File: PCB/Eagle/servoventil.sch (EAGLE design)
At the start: 0 parts

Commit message: Rozdělané schéma
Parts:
- added C1, C2: 100n 1206, rcl:C-EUC1206
- added D1: LOW BAT 1206, SparkFun-LED:LED1206
- added D2: STTH4R02S DO214AB, diode:DIODE-DO214AA
- added DIP: DIP-4X_DIP, #PaJa_prepinace:DIP-4X_DIP
- added F1: 3,5A 1206, adafruit:PTCFUSE-1206
- added IO1: ATTINY1634 SO20W, bt_avr:ATTINY1634-SU
- added IO2: MCP1825 SOT223, bt_regulator:MCP1825_SOT223
- added IO3: DS3231MZ+, SamacSys_Parts:DS3231MZ+
- added J1: ICSP 2x5, SparkFun-Connectors:AVR_SPI_PROG_5X2LOCK
- added J2: SERIAL, #PaJa_konektory:S1G5_JUMP
- added K1: ARK500/2, #PaJa_konektory:ARK500/2
- added R1, R8: 10k 1206, rcl:R-EU_R1206
- added R10, R9: 4k7 1206, rcl:R-EU_R1206
- added R2: 10k 1203, rcl:R-EU_R1206
- added R3: 1k 1206, rcl:R-EU_R1206
- added R4: 47k 1206, rcl:R-EU_R1206
- added R5: 2k7 1206, rcl:R-EU_R1206
- added R6: 3k3 1206, rcl:R-EU_R1206
- added R7: 100R 1206, rcl:R-EU_R1206
- added S1: 6x6mm SMD, SparkFun-Switches:MOMENTARY-SWITCH-SPST-SMD-6.2MM-TALL
- added T1: DMP2100U SOT23, bt_transistor:MOSFET-P-SOT23
- added T2: IRF7416PBF SO8, SamacSys_Parts:IRF7416PBF
- added T3: FDV303N SOT23, bt_transistor:MOSFET-N-SOT23
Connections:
- new net 3,3V_VCC: C2.1, IO2.VOUT, IO3.VCC, R10.1, R9.1
- new net 6V: C1.1, IO2.VIN, R5.2, T1.D
- new net GND: C1.2, C2.2, D1.C, D2.A, DIP.1, DIP.2, DIP.3, DIP.4, IO1.GND, IO3.GND, J1.GND@1, J1.GND@2, J1.GND@3, J1.GND@4, J2.1, K1.K1, R4.1, R6.1, S1.1, T3.S
- new net HEATSINK: IO2.GND, IO2.HEATSINK
- new net LED_LOWBAT_PIN: R7.1
- new net LOW_BAT_PIN: R5.1, R6.2
- new net N$1: F1.2, K1.K2
- new net N$10: IO3.!INT!/SQW
- new net N$12: D1.A, R7.2
- new net N$2: D2.C, F1.1, R1.2, R2.2, T1.S, T2.S_1, T2.S_2, T2.S_3
- new net N$3: R3.2, R4.2, T3.G
- new net N$5: J1.SCK
- new net N$6: J1.MISO
- new net N$7: J1.MOSI
- new net PWR_ON_PIN: R3.1
- new net PWR_RTC_ON: R1.1, S1.2, T1.G, T3.D
- new net PWR_SERVO_ON_PIN: R2.1, T2.G
- new net PWR_SERVO_OUT: T2.D_1, T2.D_2, T2.D_3, T2.D_4
- new net RESET: IO1.(RESET/DW/PCINT15)PC3, J1.RESET, J2.5, R8.2
- new net RX_PIN: J2.4
- new net SCL_PIN: IO3.SCL, R9.2
- new net SDA_PIN: IO3.SDA, R10.2
- new net SW1_PIN: DIP.8
- new net SW2_PIN: DIP.7
- new net SW3_PIN: DIP.6
- new net SW4_PIN: DIP.5
- new net TX_PIN: J2.3
- new net VCC: IO1.VCC, J1.VCC, J2.2, R8.1
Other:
- note added: "+ 0V"
- note added: "Baterie (5x AA 1,2V)"
- note added: "CPU"
- note added: "GND 3,3V TX RX RESET"
- note added: "PWR ON"
- note added: "RTC"
- note added: "ZDROJ"

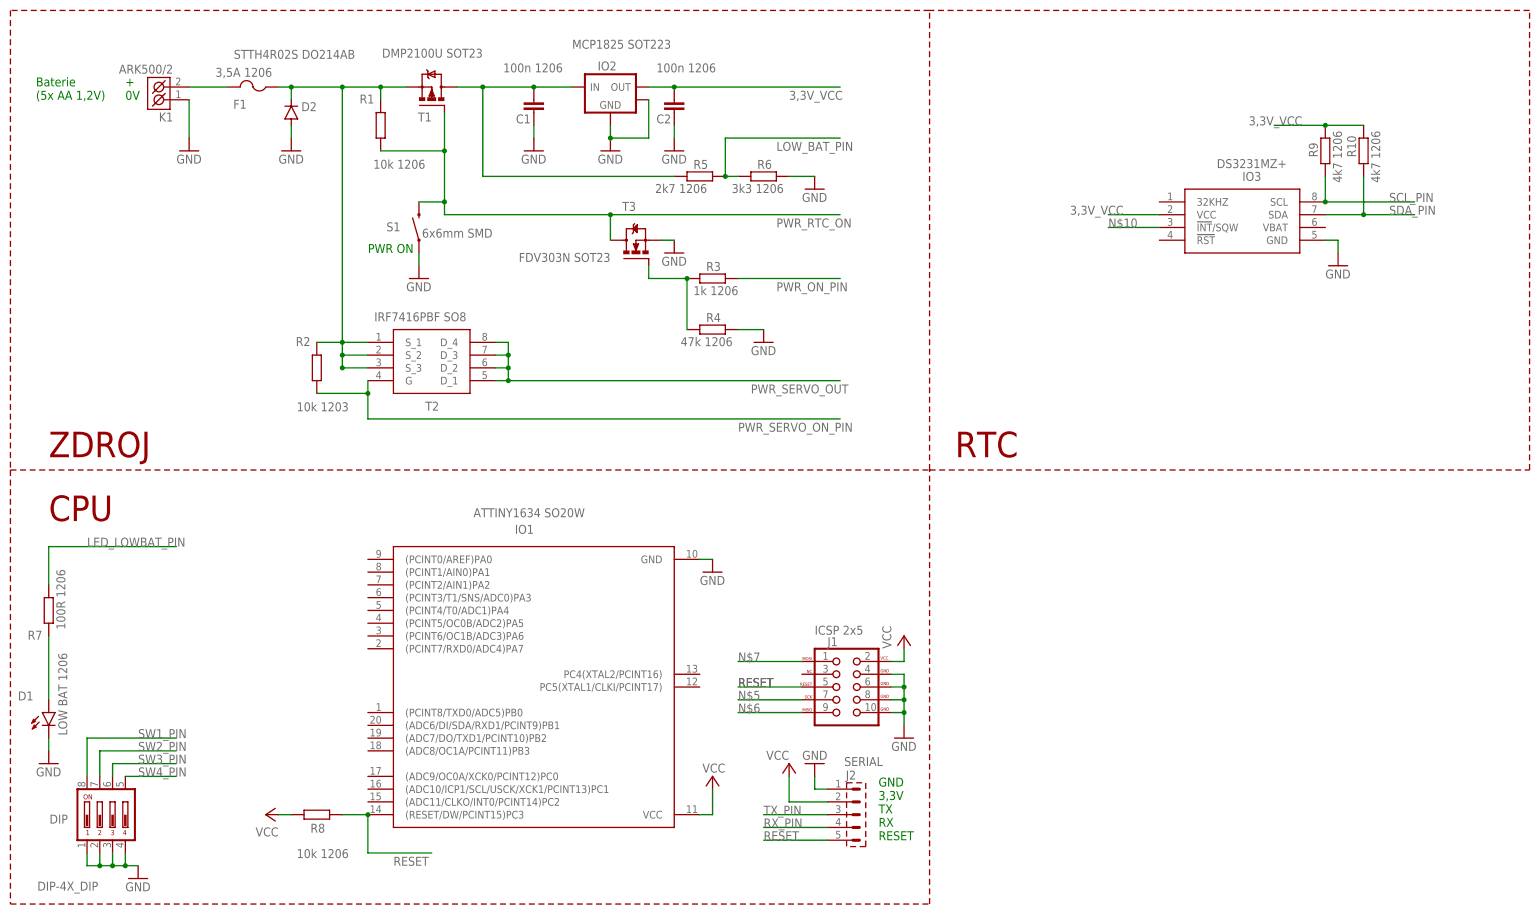
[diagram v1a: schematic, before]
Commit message: Schema před kontrolou
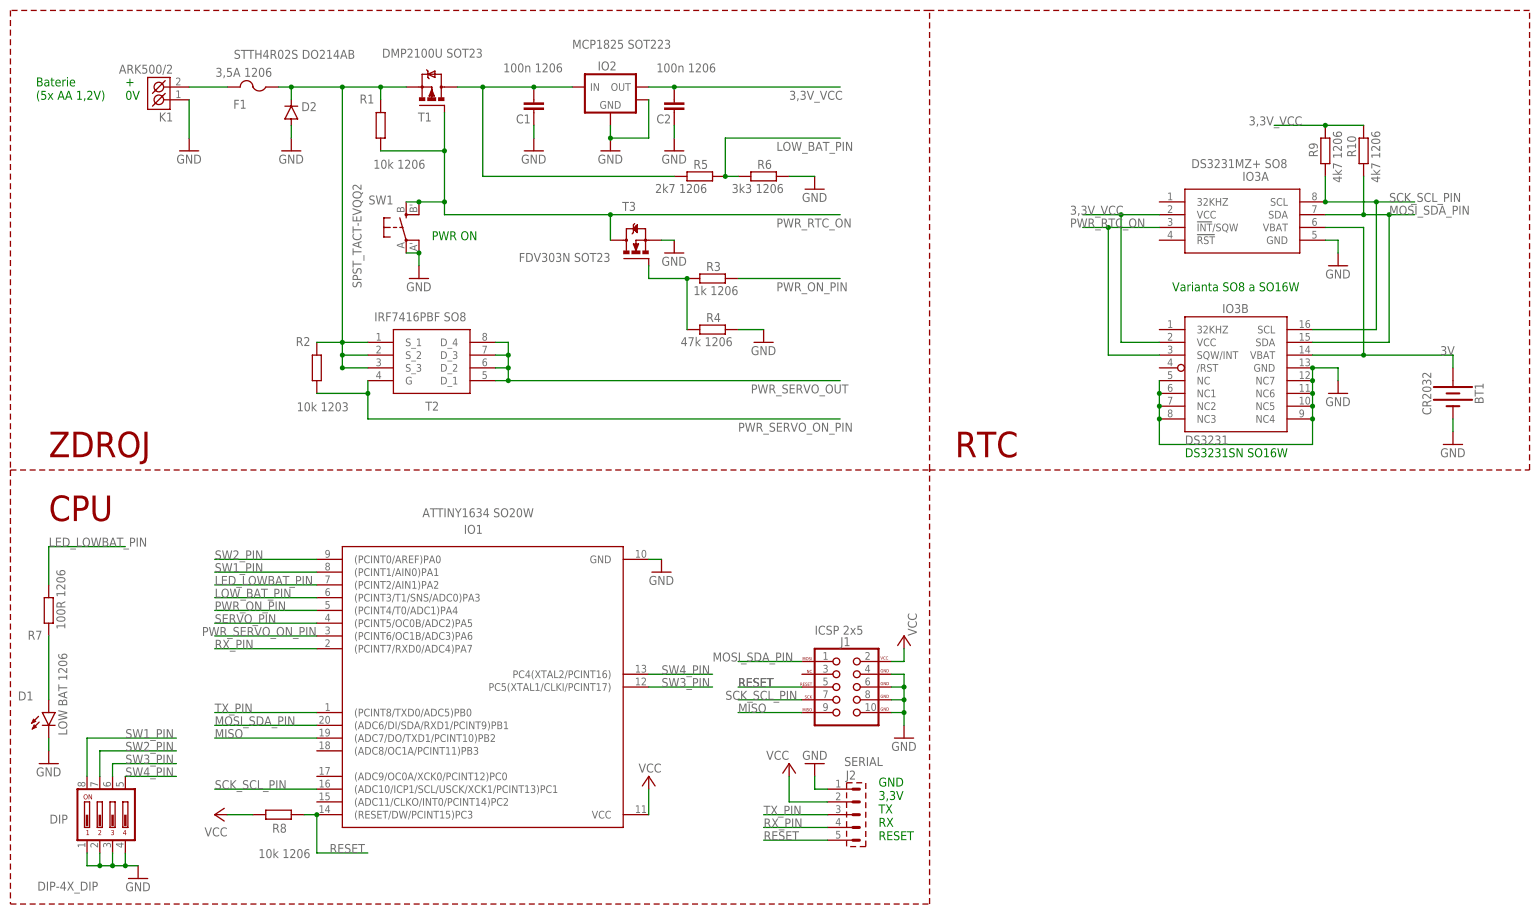
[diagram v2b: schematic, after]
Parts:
- removed S1: 6x6mm SMD, SparkFun-Switches:MOMENTARY-SWITCH-SPST-SMD-6.2MM-TALL
- added BT1: CR2032, SparkFun-Batteries:BATTERY-20MM_PTH
- added IO3B: DS3231SN SO16W, adafruit:DS3231/SO
- added SW1: SPST_TACT-EVQQ2, adafruit:SPST_TACT-EVQQ2
- IO3A: value DS3231MZ+ -> DS3231MZ+ SO8
- renumbered IO3 to IO3A
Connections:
- removed net N$10: IO3A.!INT!/SQW
- removed net N$5: J1.SCK
- removed net N$6: J1.MISO
- removed net N$7: J1.MOSI
- removed net SCL_PIN: IO3A.SCL, R9.2
- removed net SDA_PIN: IO3A.SDA, R10.2
- new net 3V: BT1.+, IO3A.VBAT, IO3B.VBAT
- new net MISO: IO1.(ADC7/DO/TXD1/PCINT10)PB2, J1.MISO
- new net MOSI_SDA_PIN: IO1.(ADC6/DI/SDA/RXD1/PCINT9)PB1, IO3A.SDA, IO3B.SDA, J1.MOSI, R10.2
- new net SCK_SCL_PIN: IO1.(ADC10/ICP1/SCL/USCK/XCK1/PCINT13)PC1, IO3A.SCL, IO3B.SCL, J1.SCK, R9.2
- new net SERVO_PIN: IO1.(PCINT5/OC0B/ADC2)PA5
- net 3,3V_VCC: now also IO3B.VCC
- net GND: now also BT1.-, IO3B.GND, IO3B.NC, IO3B.NC1, IO3B.NC2, IO3B.NC3, IO3B.NC4, IO3B.NC5, IO3B.NC6, IO3B.NC7, SW1.P, SW1.P1; no longer S1.1
- net LED_LOWBAT_PIN: now also IO1.(PCINT2/AIN1)PA2
- net LOW_BAT_PIN: now also IO1.(PCINT3/T1/SNS/ADC0)PA3
- net PWR_ON_PIN: now also IO1.(PCINT4/T0/ADC1)PA4
- net PWR_RTC_ON: now also IO3A.!INT!/SQW, IO3B.SQW/INT, SW1.S, SW1.S1; no longer S1.2
- net PWR_SERVO_ON_PIN: now also IO1.(PCINT6/OC1B/ADC3)PA6
- net RX_PIN: now also IO1.(PCINT7/RXD0/ADC4)PA7
- net SW1_PIN: now also IO1.(PCINT1/AIN0)PA1
- net SW2_PIN: now also IO1.(PCINT0/AREF)PA0
- net SW3_PIN: now also IO1.PC5(XTAL1/CLKI/PCINT17)
- net SW4_PIN: now also IO1.PC4(XTAL2/PCINT16)
- net TX_PIN: now also IO1.(PCINT8/TXD0/ADC5)PB0
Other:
- note added: "DS3231SN SO16W"
- note added: "Varianta SO8 a SO16W"
- moved on the sheet: IO1, R8

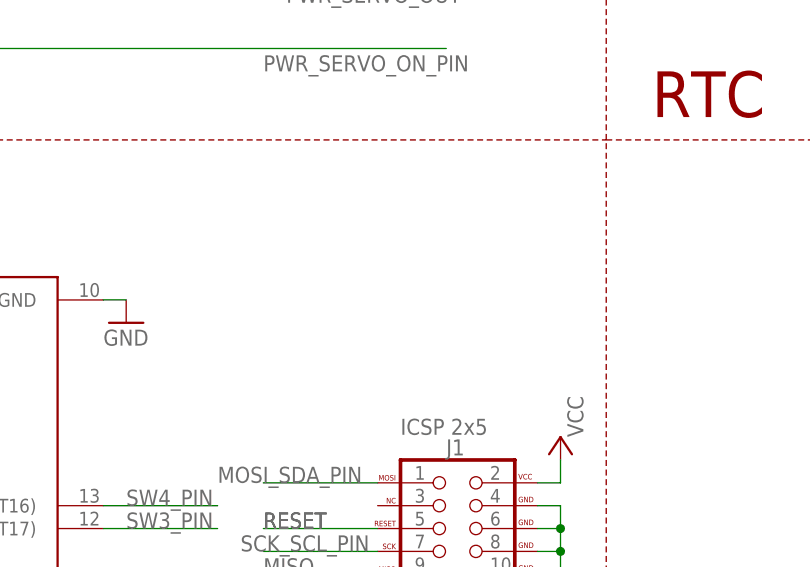
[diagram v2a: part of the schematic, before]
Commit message: Deska spojů, schéma
vše před kontrolou (až dorazí součástky)
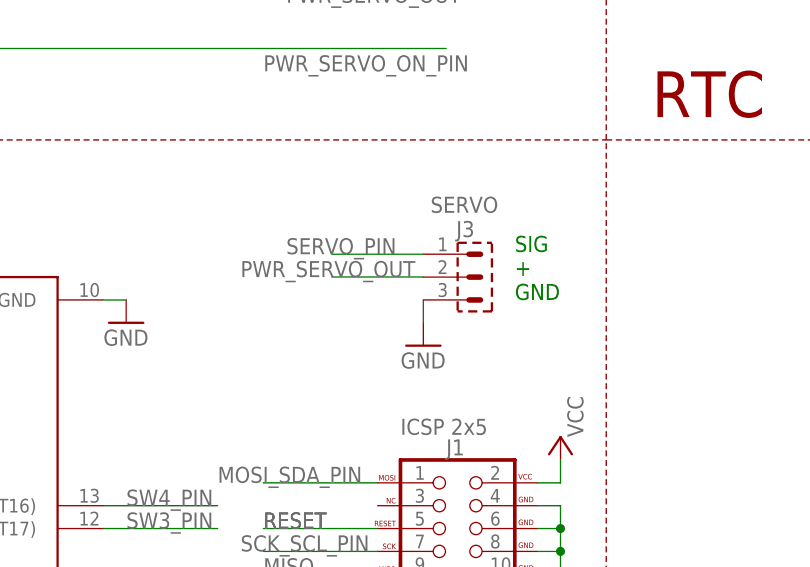
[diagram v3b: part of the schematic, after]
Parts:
- added J3: SERVO, #PaJa_konektory:S1G3_JUMP
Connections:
- net GND: now also J3.3
- net PWR_SERVO_OUT: now also J3.2
- net SERVO_PIN: now also J3.1
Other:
- note added: "SIG + GND"
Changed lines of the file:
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@@
 <part name="BT1" library="SparkFun-Batteries" deviceset="BATTERY" device="-20MM_PTH" value="CR2032"/>
 <part name="GND17" library="supply1" library_urn="urn:adsk.eagle:library:371" deviceset="GND" device=""/>
+<part name="J3" library="#PaJa_konektory" deviceset="S1G3_JUMP" device="" value="SERVO"/>
+<part name="GND18" library="supply1" library_urn="urn:adsk.eagle:library:371" deviceset="GND" device=""/>
 </parts>
 <sheets>
@@
 <text x="208.28" y="71.12" size="1.778" layer="91">Varianta SO8 a SO16W</text>
 <text x="210.82" y="38.1" size="1.778" layer="91">DS3231SN SO16W</text>
+<text x="149.86" y="17.78" size="1.778" layer="91">SIG
++
+GND</text>
 </plain>
 <instances>
@@
 <instance part="GND17" gate="1" x="264.16" y="40.64" smashed="yes">
 <attribute name="VALUE" x="261.62" y="38.1" size="1.778" layer="96"/>
+</instance>
+<instance part="J3" gate="JUMP" x="142.24" y="20.32" smashed="yes" rot="R270">
+<attribute name="PART" x="143.3512" y="24.765" size="1.778" layer="95" font="vector"/>
+<attribute name="VALUE" x="140.4937" y="27.4638" size="1.778" layer="96" font="vector"/>
+</instance>
+<instance part="GND18" gate="1" x="139.7" y="12.7" smashed="yes">
+<attribute name="VALUE" x="137.16" y="10.16" size="1.778" layer="96"/>
 </instance>
 </instances>
@@
 <wire x1="264.16" y1="45.72" x2="264.16" y2="43.18" width="0.1524" layer="91"/>
 </segment>
+<segment>
+<pinref part="J3" gate="JUMP" pin="3"/>
+<pinref part="GND18" gate="1" pin="GND"/>
+<wire x1="139.7" y1="17.78" x2="139.7" y2="15.24" width="0.1524" layer="91"/>
+</segment>
 </net>
 <net name="N$1" class="0">
@@
 <wire x1="76.2" y1="53.34" x2="142.24" y2="53.34" width="0.1524" layer="91"/>
 </segment>
+<segment>
+<pinref part="J3" gate="JUMP" pin="2"/>
+<wire x1="139.7" y1="20.32" x2="129.54" y2="20.32" width="0.1524" layer="91"/>
+<label x="119.38" y="20.32" size="1.778" layer="95"/>
+</segment>
 </net>
 <net name="PWR_SERVO_ON_PIN" class="0">
@@
 <label x="17.78" y="5.08" size="1.778" layer="95"/>
 </segment>
-</net>
+<segment>
+<pinref part="J3" gate="JUMP" pin="1"/>
+<wire x1="139.7" y1="22.86" x2="129.54" y2="22.86" width="0.1524" layer="91"/>
+<label x="124.46" y="22.86" size="1.778" layer="95"/>
+</segment>
+</net>

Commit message: Schéma a deska před kontrolou
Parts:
- added J4: I2C, #PaJa_konektory:S1G4_JUMP
- added R11: 1k 1206, rcl:R-EU_R1206
- added R12: 47k 1206, rcl:R-EU_R1206
- added T4: FDV303N SOT23, bt_transistor:MOSFET-N-SOT23
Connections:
- removed net 3,3V_VCC: C2.1, IO2.VOUT, IO3A.VCC, IO3B.VCC, R10.1, R9.1
- new net N$4: R2.1, T2.G, T4.D
- new net N$5: R11.2, R12.2, T4.G
- net GND: now also J4.1, R12.1, T4.S
- net MOSI_SDA_PIN: now also J4.3
- net PWR_SERVO_ON_PIN: now also R11.1; no longer R2.1, T2.G
- net SCK_SCL_PIN: now also J4.4
- net VCC: now also C2.1, IO2.VOUT, IO3A.VCC, IO3B.VCC, J4.2, R10.1, R9.1
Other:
- note added: "SCL SDA 3,3V GND"

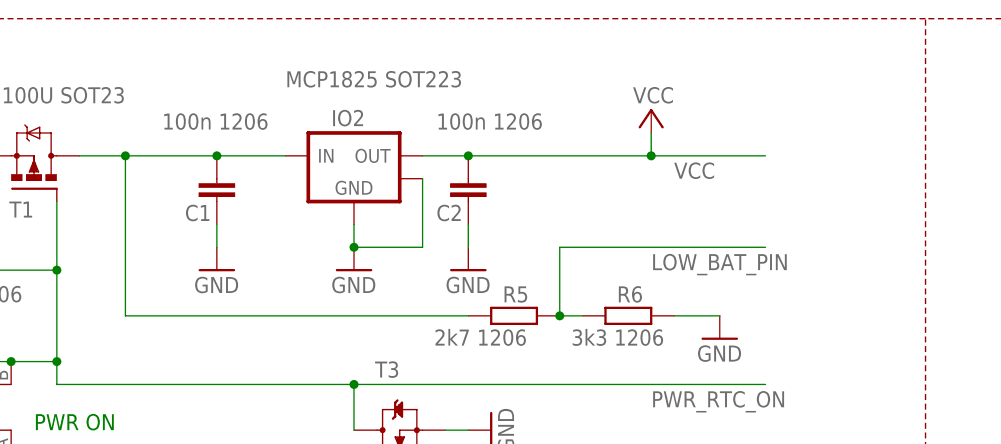
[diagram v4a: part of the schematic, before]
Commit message: oprava chyby na desce
chyběla zem pod 3,3V stabilizátorem (heatsink + gnd se nespojilo)
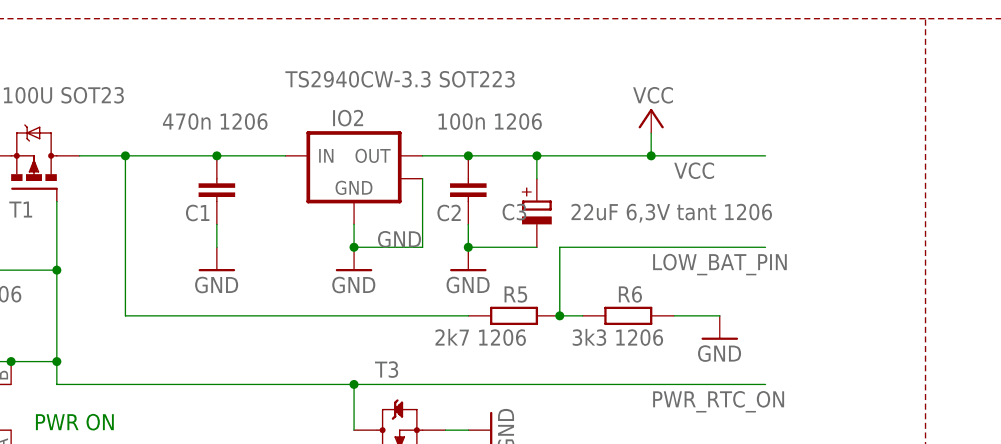
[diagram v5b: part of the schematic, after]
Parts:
- added C3: 22uF 6,3V tant 1206, rcl:CPOL-EUCT3216
- C1: value 100n 1206 -> 470n 1206
- IO2: value MCP1825 SOT223 -> TS2940CW-3.3 SOT223
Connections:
- removed net HEATSINK: IO2.GND, IO2.HEATSINK
- net GND: now also C3.-, IO2.GND, IO2.HEATSINK
- net VCC: now also C3.+
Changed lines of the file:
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@@
 <part name="GND1" library="supply1" library_urn="urn:adsk.eagle:library:371" deviceset="GND" device=""/>
 <part name="P+1" library="supply1" library_urn="urn:adsk.eagle:library:371" deviceset="VCC" device=""/>
-<part name="IO2" library="bt_regulator" deviceset="MCP1825" device="_SOT223" value="MCP1825 SOT223"/>
+<part name="IO2" library="bt_regulator" deviceset="MCP1825" device="_SOT223" value="TS2940CW-3.3 SOT223"/>
 <part name="T1" library="bt_transistor" deviceset="MOSFET-P" device="-SOT23" value="DMP2100U SOT23"/>
 <part name="T3" library="bt_transistor" deviceset="MOSFET-N" device="-SOT23" value="FDV303N SOT23"/>
@@
 <part name="F1" library="adafruit" library_urn="urn:adsk.eagle:library:420" deviceset="PTCFUSE" device="-1206" package3d_urn="urn:adsk.eagle:package:6240569/1" value="3,5A 1206"/>
 <part name="D2" library="diode" library_urn="urn:adsk.eagle:library:210" deviceset="DIODE-" device="DO214AA" package3d_urn="urn:adsk.eagle:package:43433/2" value="STTH4R02S  DO214AB"/>
-<part name="C1" library="rcl" library_urn="urn:adsk.eagle:library:334" deviceset="C-EU" device="C1206" package3d_urn="urn:adsk.eagle:package:23618/2" value="100n 1206"/>
+<part name="C1" library="rcl" library_urn="urn:adsk.eagle:library:334" deviceset="C-EU" device="C1206" package3d_urn="urn:adsk.eagle:package:23618/2" value="470n 1206"/>
 <part name="C2" library="rcl" library_urn="urn:adsk.eagle:library:334" deviceset="C-EU" device="C1206" package3d_urn="urn:adsk.eagle:package:23618/2" value="100n 1206"/>
 <part name="R1" library="rcl" library_urn="urn:adsk.eagle:library:334" deviceset="R-EU_" device="R1206" package3d_urn="urn:adsk.eagle:package:23540/2" value="10k 1206"/>
@@
 <part name="P+7" library="supply1" library_urn="urn:adsk.eagle:library:371" deviceset="VCC" device=""/>
 <part name="P+8" library="supply1" library_urn="urn:adsk.eagle:library:371" deviceset="VCC" device=""/>
+<part name="C3" library="rcl" library_urn="urn:adsk.eagle:library:334" deviceset="CPOL-EU" device="CT3216" package3d_urn="urn:adsk.eagle:package:23327/2" value="22uF 6,3V tant 1206"/>
 </parts>
 <sheets>
@@
 <attribute name="VALUE" x="200.66" y="96.52" size="1.778" layer="96" rot="R180"/>
 </instance>
+<instance part="C3" gate="G$1" x="116.84" y="106.68" smashed="yes">
+<attribute name="NAME" x="112.903" y="104.6226" size="1.778" layer="95"/>
+<attribute name="VALUE" x="120.523" y="104.6226" size="1.778" layer="96"/>
+</instance>
 </instances>
 <busses>
@@
 <pinref part="C2" gate="G$1" pin="1"/>
 <wire x1="104.14" y1="111.76" x2="109.22" y2="111.76" width="0.1524" layer="91"/>
-<wire x1="109.22" y1="111.76" x2="129.54" y2="111.76" width="0.1524" layer="91"/>
+<wire x1="109.22" y1="111.76" x2="116.84" y2="111.76" width="0.1524" layer="91"/>
 <junction x="109.22" y="111.76"/>
 <label x="132.08" y="109.22" size="1.778" layer="95"/>
 <pinref part="P+5" gate="VCC" pin="VCC"/>
+<wire x1="116.84" y1="111.76" x2="129.54" y2="111.76" width="0.1524" layer="91"/>
 <wire x1="129.54" y1="111.76" x2="142.24" y2="111.76" width="0.1524" layer="91"/>
 <wire x1="129.54" y1="114.3" x2="129.54" y2="111.76" width="0.1524" layer="91"/>
 <junction x="129.54" y="111.76"/>
+<pinref part="C3" gate="G$1" pin="+"/>
+<wire x1="116.84" y1="109.22" x2="116.84" y2="111.76" width="0.1524" layer="91"/>
+<junction x="116.84" y="111.76"/>
 </segment>
 <segment>
@@
 <pinref part="GND6" gate="1" pin="GND"/>
 <wire x1="109.22" y1="104.14" x2="109.22" y2="101.6" width="0.1524" layer="91"/>
+<pinref part="C3" gate="G$1" pin="-"/>
+<wire x1="116.84" y1="101.6" x2="109.22" y2="101.6" width="0.1524" layer="91"/>
+<junction x="109.22" y="101.6"/>
 </segment>
 <segment>
@@
 <wire x1="185.42" y1="104.14" x2="185.42" y2="101.6" width="0.1524" layer="91"/>
 </segment>
+<segment>
+<pinref part="IO2" gate="&gt;NAME" pin="HEATSINK"/>
+<wire x1="104.14" y1="109.22" x2="104.14" y2="101.6" width="0.1524" layer="91"/>
+<pinref part="IO2" gate="&gt;NAME" pin="GND"/>
+<pinref part="GND5" gate="1" pin="GND"/>
+<wire x1="96.52" y1="104.14" x2="96.52" y2="101.6" width="0.1524" layer="91"/>
+<wire x1="104.14" y1="101.6" x2="96.52" y2="101.6" width="0.1524" layer="91"/>
+<junction x="96.52" y="101.6"/>
+<label x="99.06" y="101.6" size="1.778" layer="95"/>
+</segment>
 </net>
 <net name="N$1" class="0">
@@
 </segment>
 </net>
-<net name="HEATSINK" class="0">
-<segment>
-<pinref part="IO2" gate="&gt;NAME" pin="HEATSINK"/>
-<wire x1="104.14" y1="109.22" x2="104.14" y2="101.6" width="0.1524" layer="91"/>
-<pinref part="IO2" gate="&gt;NAME" pin="GND"/>
-<pinref part="GND5" gate="1" pin="GND"/>
-<wire x1="96.52" y1="104.14" x2="96.52" y2="101.6" width="0.1524" layer="91"/>
-<wire x1="104.14" y1="101.6" x2="96.52" y2="101.6" width="0.1524" layer="91"/>
-<junction x="96.52" y="101.6"/>
-</segment>
-</net>
